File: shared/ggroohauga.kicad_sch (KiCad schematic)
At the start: 6 parts

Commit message: Rotate MOSFET pins so that it's connected correctly
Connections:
- net +3.3V: now also C-Q1.2 (S); no longer C-Q1.3 (S)
- net CON_POWER_OUT: now also C-Q1.3 (D); no longer C-Q1.1 (D)
- net GPIO_L40_C40_M41/CON_POWER_OUT: now also C-Q1.1 (G); no longer C-Q1.2 (G)
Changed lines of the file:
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@@
 			)
 		)
-		(property "Sim.Pins" "1=D 2=G 3=S"
+		(property "Sim.Pins" "1=G 2=S 3=D"
 			(at 256.54 73.66 0)
 			(effects

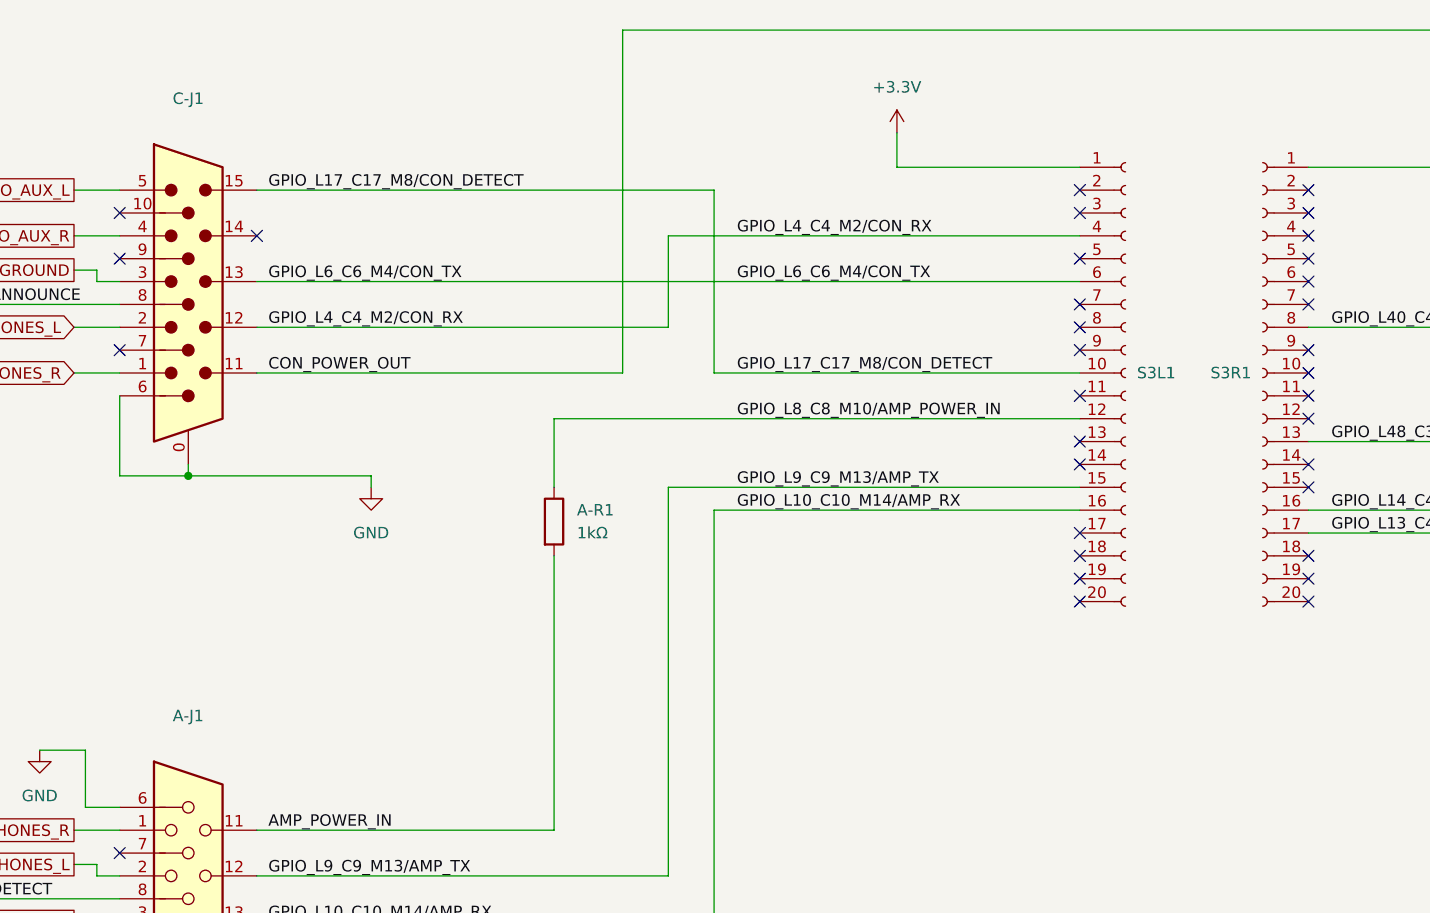
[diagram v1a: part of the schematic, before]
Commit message: Convert to KiCad 9.0 format
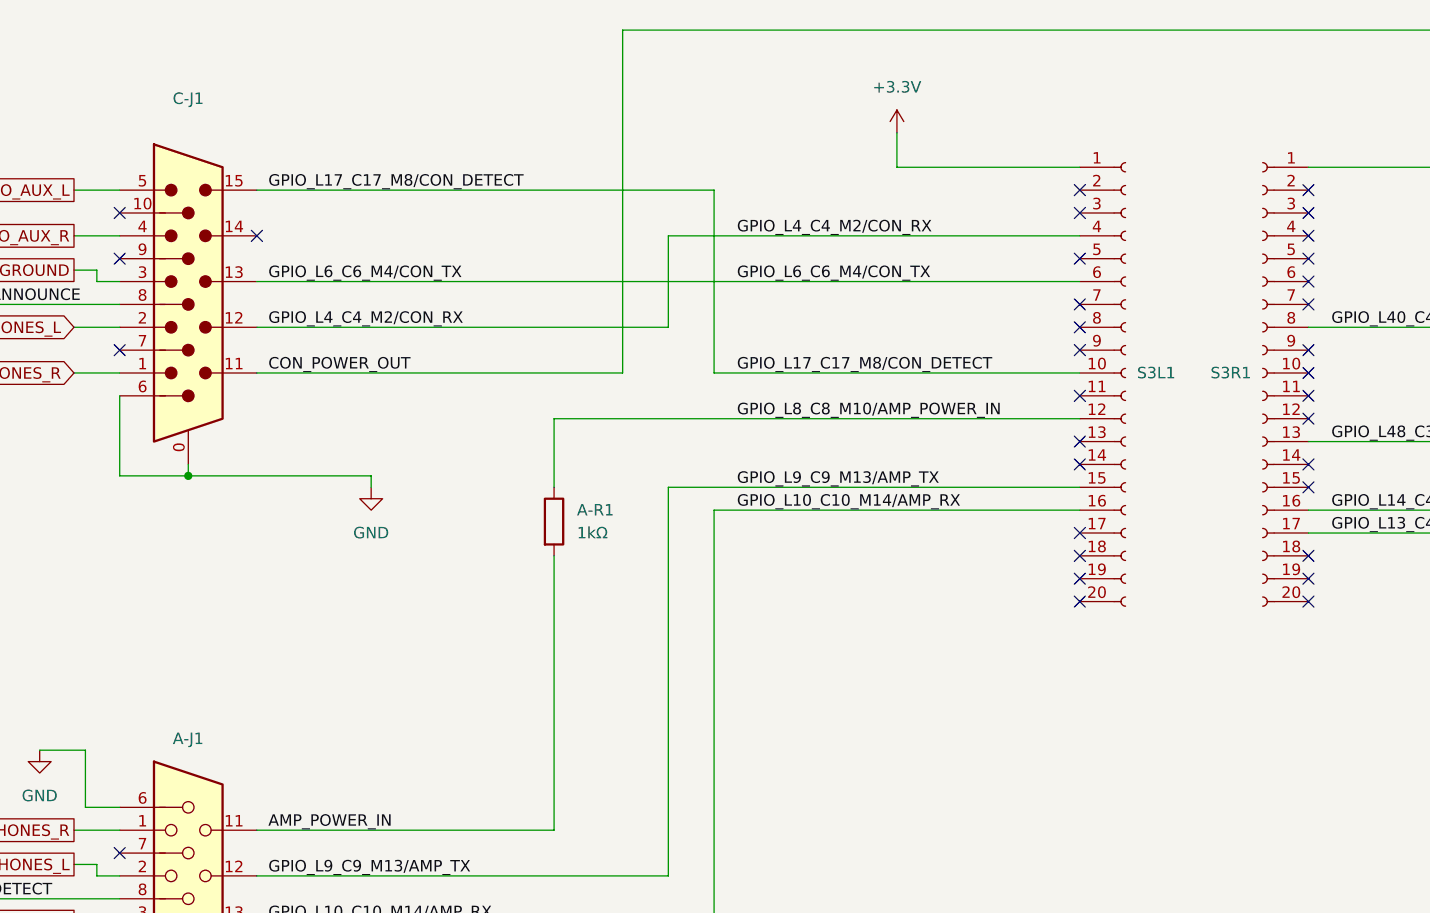
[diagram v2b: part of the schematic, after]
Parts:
- A-J1: value DE15_Receptacle_HighDensity_MountingHoles -> DE15_Socket_HighDensity_MountingHoles; symbol Connector:DE15_Receptacle_HighDensity_MountingHoles -> Connector:DE15_Socket_HighDensity_MountingHoles
- C-J1: value DE15_Plug_HighDensity_MountingHoles -> DE15_Pins_HighDensity_MountingHoles; symbol Connector:DE15_Plug_HighDensity_MountingHoles -> Connector:DE15_Pins_HighDensity_MountingHoles
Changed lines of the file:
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@@
 (kicad_sch
-	(version 20231120)
+	(version 20250114)
 	(generator "eeschema")
-	(generator_version "8.0")
+	(generator_version "9.0")
 	(paper "A4")
 	(junction
@@
 	)
 	(symbol
-		(lib_id "Connector:DE15_Receptacle_HighDensity_MountingHoles")
+		(lib_id "Connector:DE15_Socket_HighDensity_MountingHoles")
 		(at 66.04 124.46 0)
 		(unit 1)
@@
 		(fields_autoplaced yes)
 		(property "Reference" "A-J1"
-			(at 66.04 101.6 0)
-			(effects
-				(font
-					(size 1.27 1.27)
-				)
-			)
-		)
-		(property "Value" "DE15_Receptacle_HighDensity_MountingHoles"
+			(at 66.04 104.14 0)
+			(effects
+				(font
+					(size 1.27 1.27)
+				)
+			)
+		)
+		(property "Value" "DE15_Socket_HighDensity_MountingHoles"
 			(at 66.04 104.14 0)
 			(effects
@@
 			)
 		)
-		(property "Description" "15-pin female receptacle socket D-SUB connector, High density (3 columns), Triple Row, Generic, VGA-connector, Mounting Hole"
+		(property "Description" "15-pin D-SUB connector, socket (female), High density (3 columns), Triple Row, Generic, VGA-connector, Mounting Hole"
 			(at 66.04 124.46 0)
 			(effects
@@
 	)
 	(symbol
-		(lib_id "Connector:DE15_Plug_HighDensity_MountingHoles")
+		(lib_id "Connector:DE15_Pins_HighDensity_MountingHoles")
 		(at 66.04 55.88 0)
 		(unit 1)
@@
 			)
 		)
-		(property "Value" "DE15_Plug_HighDensity_MountingHoles"
+		(property "Value" "DE15_Pins_HighDensity_MountingHoles"
 			(at 66.04 35.56 0)
 			(effects
@@
 		)
 	)
+	(embedded_fonts no)
 )

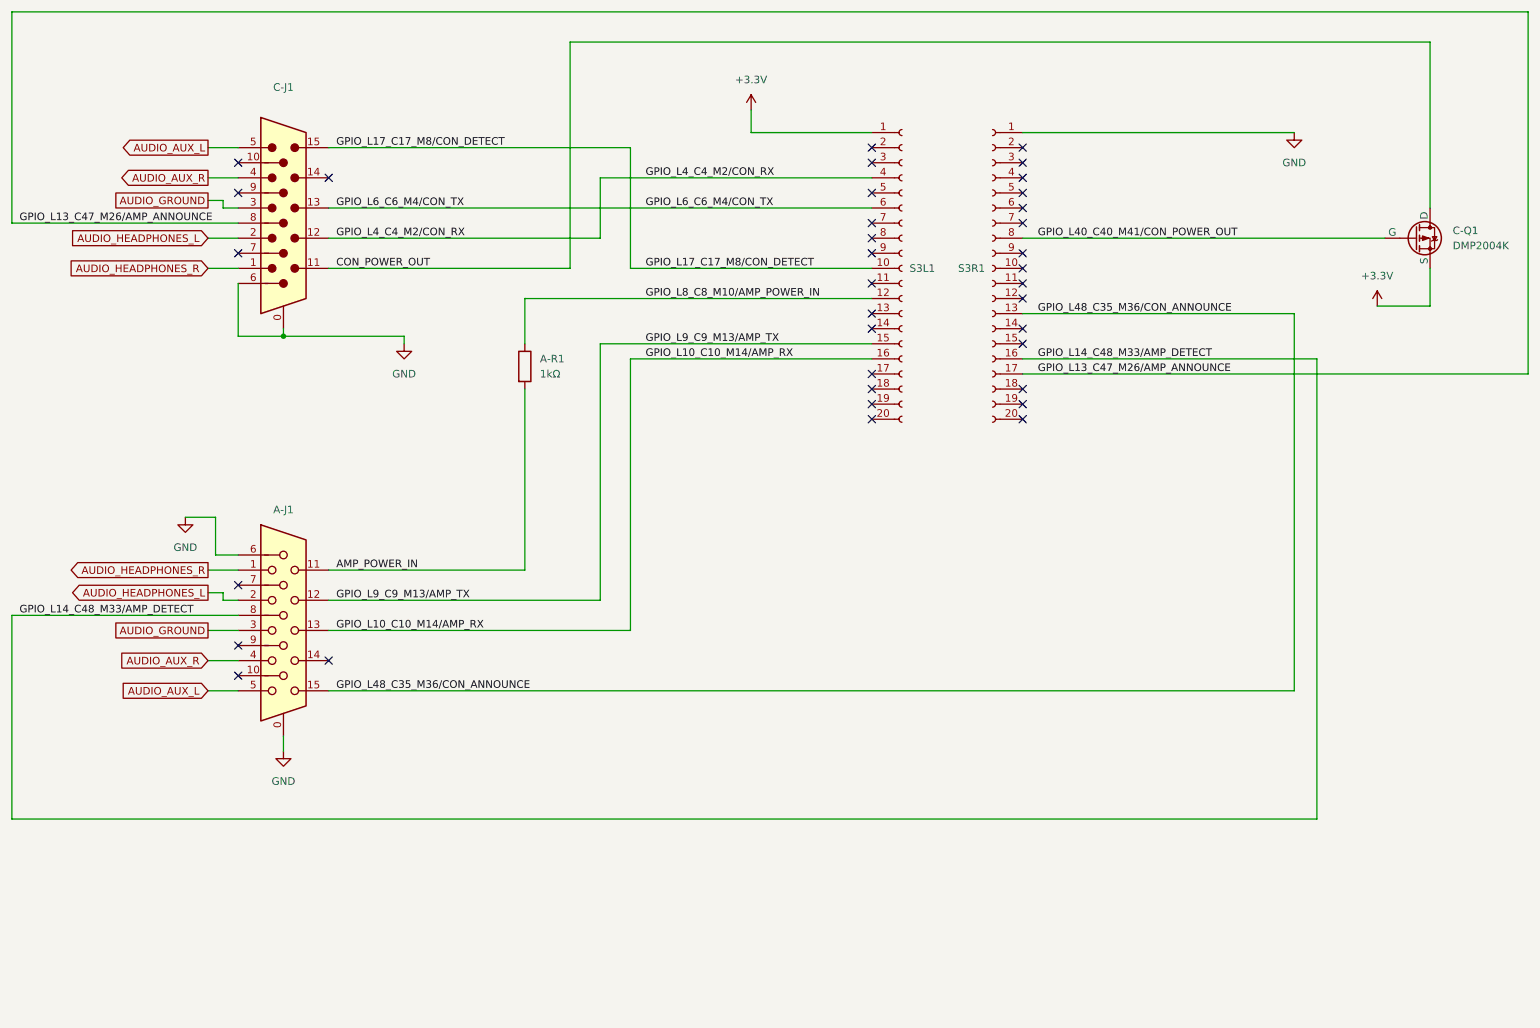
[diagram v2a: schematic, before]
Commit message: Add 4ch digital isolator and 2 TRS jacks to the schematic
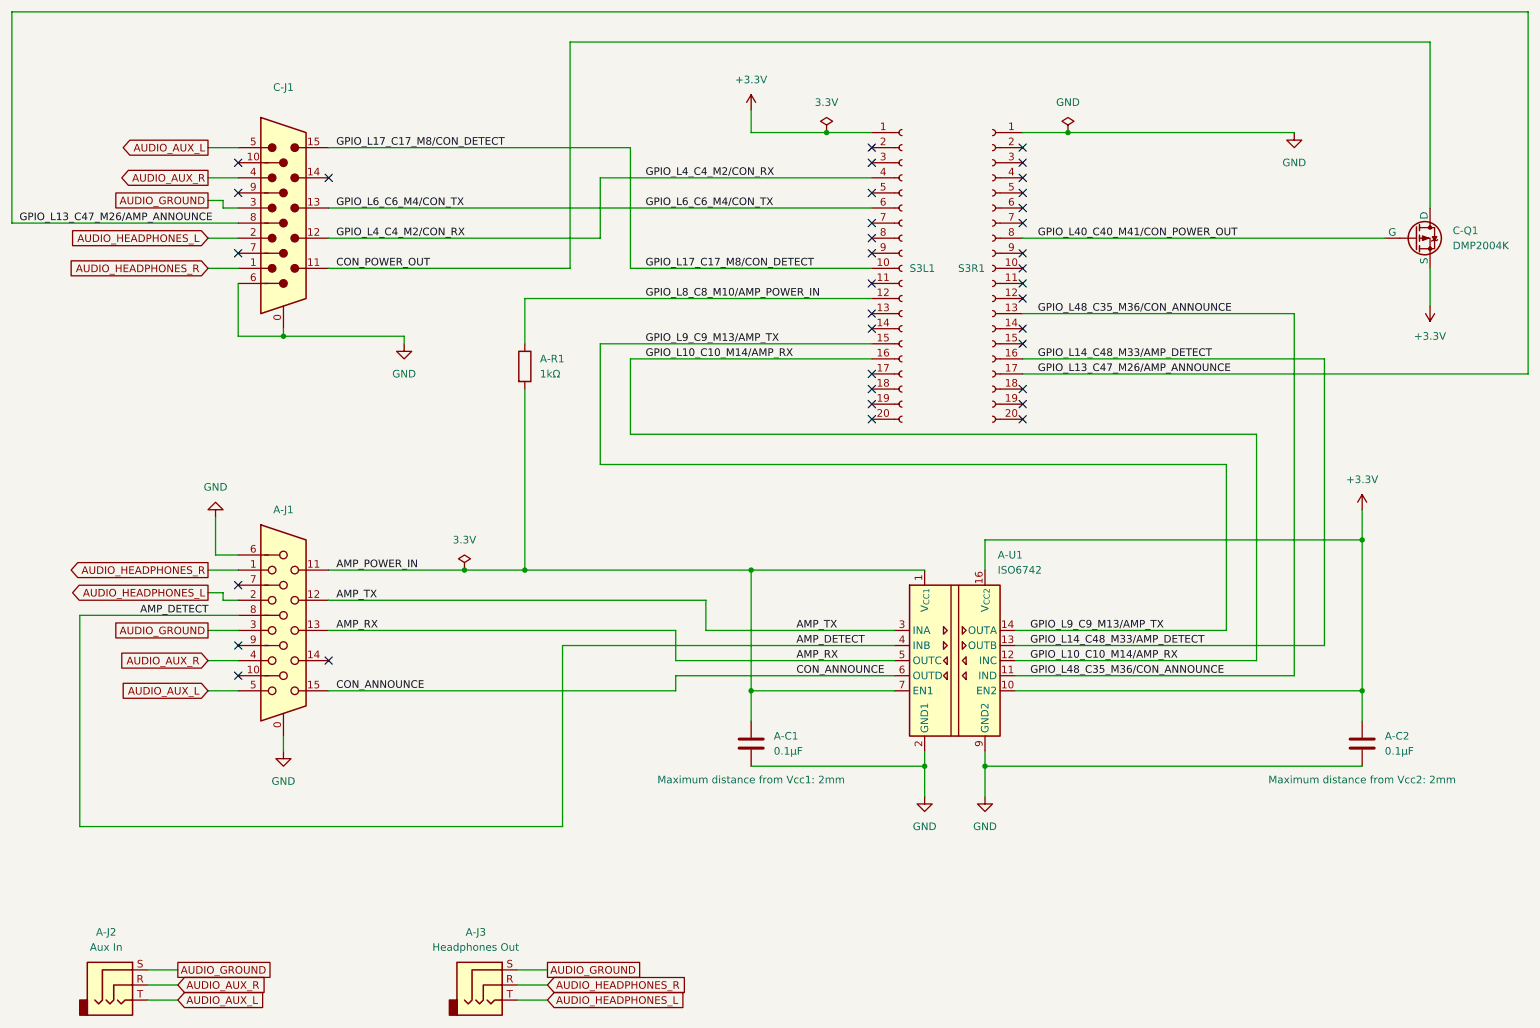
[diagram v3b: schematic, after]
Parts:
- added A-C1, A-C2: 0.1µF, Capacitor_SMD:C_0805_2012Metric_Pad1.18x1.45mm_HandSolder, symbol Device:C
- added A-J2: Aux In, Connector_Audio:Jack_3.5mm_CUI_SJ1-3523N_Horizontal, symbol Connector_Audio:AudioJack3
- added A-J3: Headphones Out, Connector_Audio:Jack_3.5mm_CUI_SJ1-3523N_Horizontal, symbol Connector_Audio:AudioJack3
- added A-U1: ISO6742, Package_SO:SOIC-16W_7.5x10.3mm_P1.27mm, symbol Isolator:ISO6742
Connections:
- net +3.3V: now also A-C2.1, A-U1.10 (EN2), A-U1.16 (V_{CC2})
- net AMP_POWER_IN: now also A-C1.1, A-U1.1 (V_{CC1}), A-U1.7 (EN1)
- net AUDIO_AUX_L: now also A-J2.T
- net AUDIO_AUX_R: now also A-J2.R
- net AUDIO_GROUND: now also A-J2.S, A-J3.S
- net AUDIO_HEADPHONES_L: now also A-J3.T
- net AUDIO_HEADPHONES_R: now also A-J3.R
- net GND: now also A-C1.2, A-C2.2, A-U1.15 (GND2), A-U1.2 (GND1), A-U1.8 (GND1), A-U1.9 (GND2)
- net GPIO_L10_C10_M14/AMP_RX: now also A-U1.12 (INC); no longer A-J1.13
- net GPIO_L14_C48_M33/AMP_DETECT: now also A-U1.13 (OUTB); no longer A-J1.8
- net GPIO_L48_C35_M36/CON_ANNOUNCE: now also A-U1.11 (IND); no longer A-J1.15
- net GPIO_L9_C9_M13/AMP_TX: now also A-U1.14 (OUTA); no longer A-J1.12
- new net AMP_DETECT: A-J1.8, A-U1.4 (INB)
- new net AMP_RX: A-J1.13, A-U1.5 (OUTC)
- new net AMP_TX: A-J1.12, A-U1.3 (INA)
- new net CON_ANNOUNCE: A-J1.15, A-U1.6 (OUTD)
